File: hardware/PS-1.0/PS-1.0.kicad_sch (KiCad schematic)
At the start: 46 parts, among them J1 Conn_02x16_Odd_Even, J2 Conn_01x05, J3 Conn_01x05, J8 Conn_01x03, J9 Conn_01x03, K1 RAYEX-L90, K2 RAYEX-L90, Q1 IRFPE50, Q2 IRFPE50, Q3 IRFPE50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

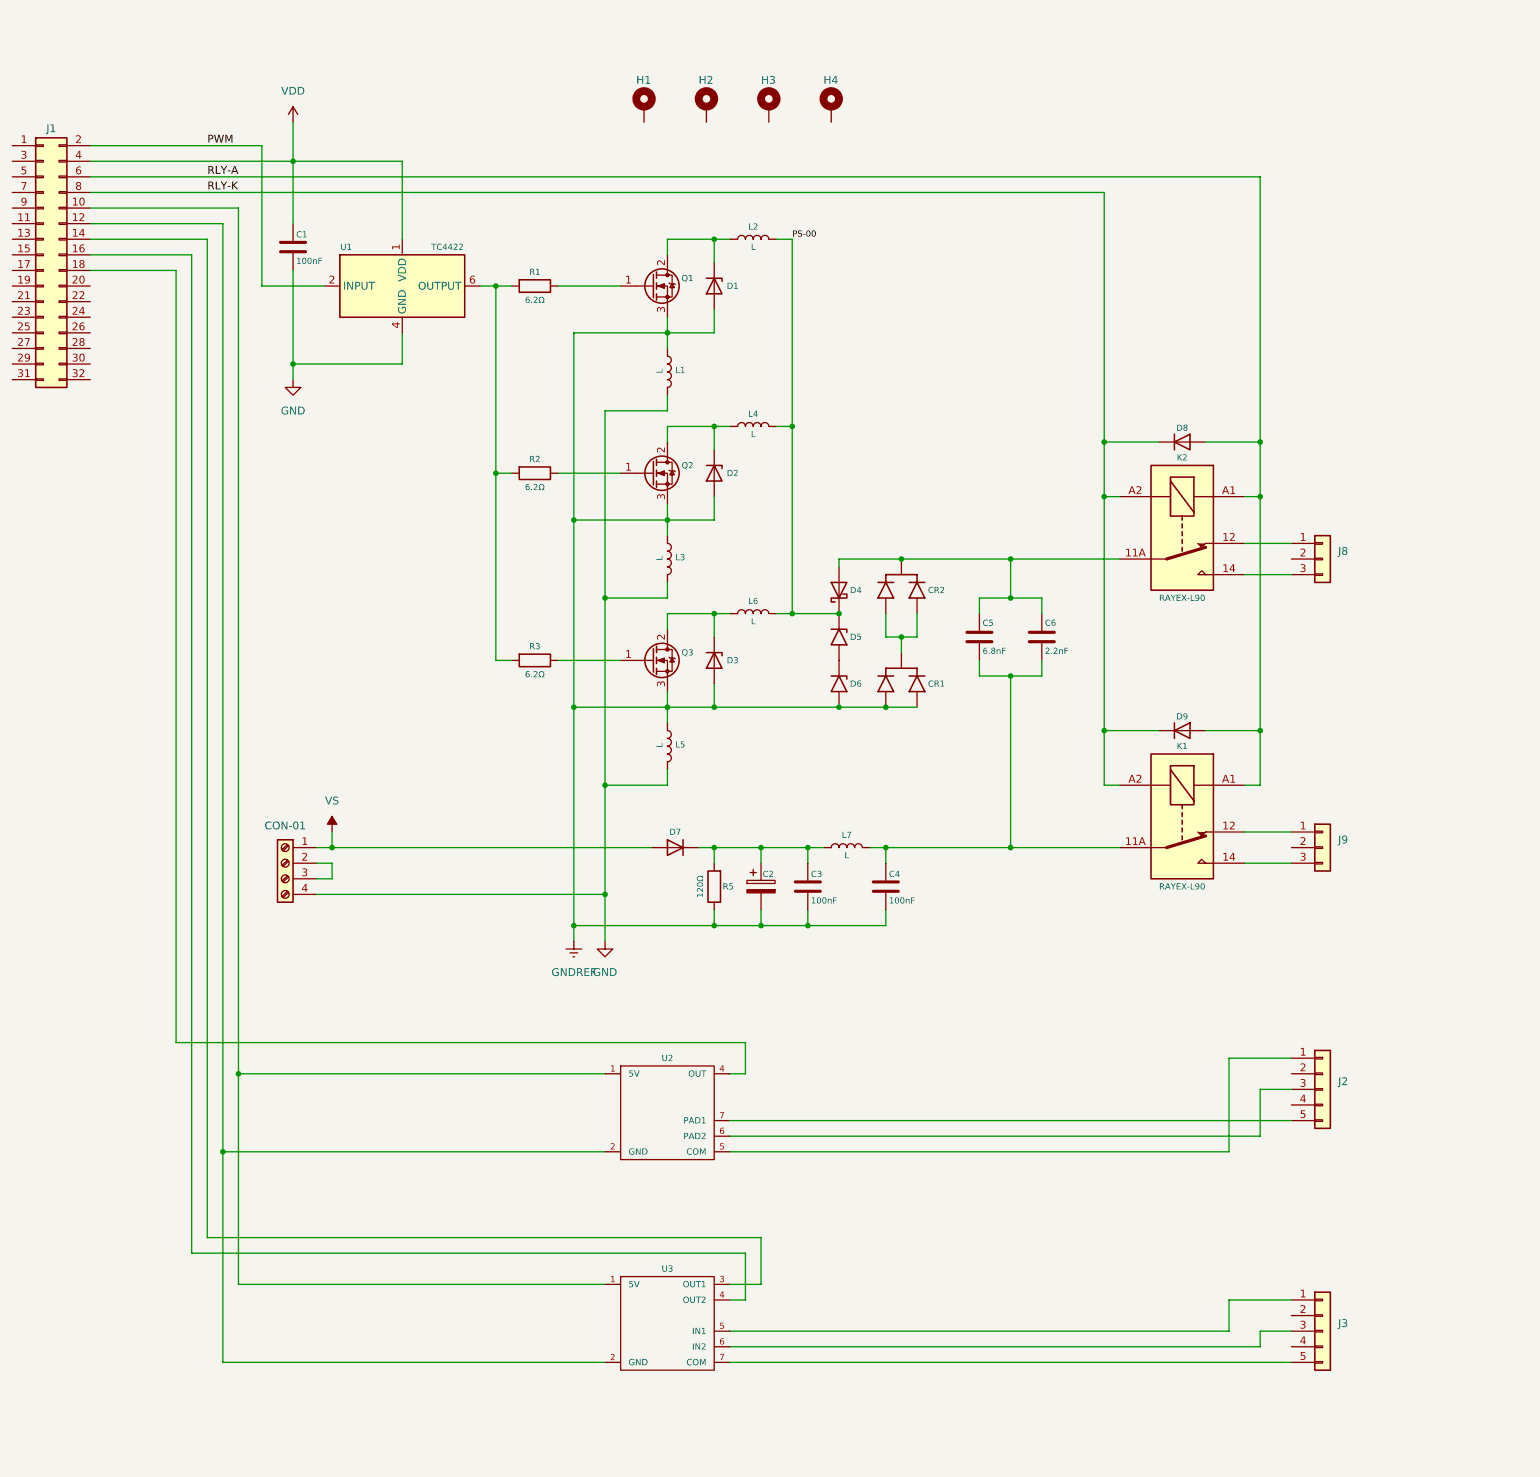
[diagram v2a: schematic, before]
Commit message: new file:   hardware/Gain/Gain-backups/Gain-2025-04-17_151501.zip 	deleted:    hardware/MSD-1.0/MSD-1.0-backups/MSD-1.0-2025-03-25_151318.zip 	deleted:    hardware/MSD-1.0/MSD-1.0-backups/MSD-1.0-2025-03-26_084506.zip 	deleted:    hardware/MSD-1.0/MSD-1.0-backups/MSD-1.0-2025-03-26_085636.zip 	deleted:    hardware/MSD-1.0/MSD-1.0-backups/MSD-1.0-2025-03-26_090649.zip 	new file:   hardware/MSD-1.0/MSD-1.0-backups/MSD-1.0-2025-04-17_090027.zip 	new file:   hardware/MSD-1.0/MSD-1.0-backups/MSD-1.0-2025-04-17_092653.zip 	new file:   hardware/MSD-1.0/MSD-1.0-backups/MSD-1.0-2025-04-17_105503.zip 	new file:   hardware/MSD-1.0/MSD-1.0-backups/MSD-1.0-2025-04-17_154051.zip 	modified:   hardware/MSD-1.0/MSD-1.0.kicad_pcb 	modified:   hardware/MSD-1.0/MSD-1.0.step 	deleted:    hardware/PS-1.0/PS-1.0-backups/PS-1.0-2025-03-19_103853.zip 	deleted:    hardware/PS-1.0/PS-1.0-backups/PS-1.0-2025-03-19_155128.zip 	deleted:    hardware/PS-1.0/PS-1.0-backups/PS-1.0-2025-03-24_095559.zip 	deleted:    hardware/PS-1.0/PS-1.0-backups/PS-1.0-2025-03-24_110339.zip 	deleted:    hardware/PS-1.0/PS-1.0-backups/PS-1.0-2025-03-24_111100.zip 	deleted:    hardware/PS-1.0/PS-1.0-backups/PS-1.0-2025-04-16_154157.zip 	deleted:    hardware/PS-1.0/PS-1.0-backups/PS-1.0-2025-04-16_154838.zip 	new file:   hardware/PS-1.0/PS-1.0-backups/PS-1.0-2025-04-16_163259.zip 	new file:   hardware/PS-1.0/PS-1.0-backups/PS-1.0-2025-04-17_105409.zip 	new file:   hardware/PS-1.0/PS-1.0-backups/PS-1.0-2025-04-17_110908.zip 	new file:   hardware/PS-1.0/PS-1.0-backups/PS-1.0-2025-04-17_114838.zip 	new file:   hardware/PS-1.0/PS-1.0-backups/PS-1.0-2025-04-17_155117.zip 	new file:   hardware/PS-1.0/PS-1.0-backups/PS-1.0-2025-04-17_155935.zip 	new file:   hardware/PS-1.0/PS-1.0-backups/PS-1.0-2025-04-17_160519.zip 	modified:   hardware/PS-1.0/PS-1.0.kicad_pcb 	modified:   hardware/PS-1.0/PS-1.0.kicad_prl 	modified:   hardware/PS-1.0/PS-1.0.kicad_pro 	modified:   hardware/PS-1.0/PS-1.0.kicad_sch 	modified:   hardware/PS-1.0/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
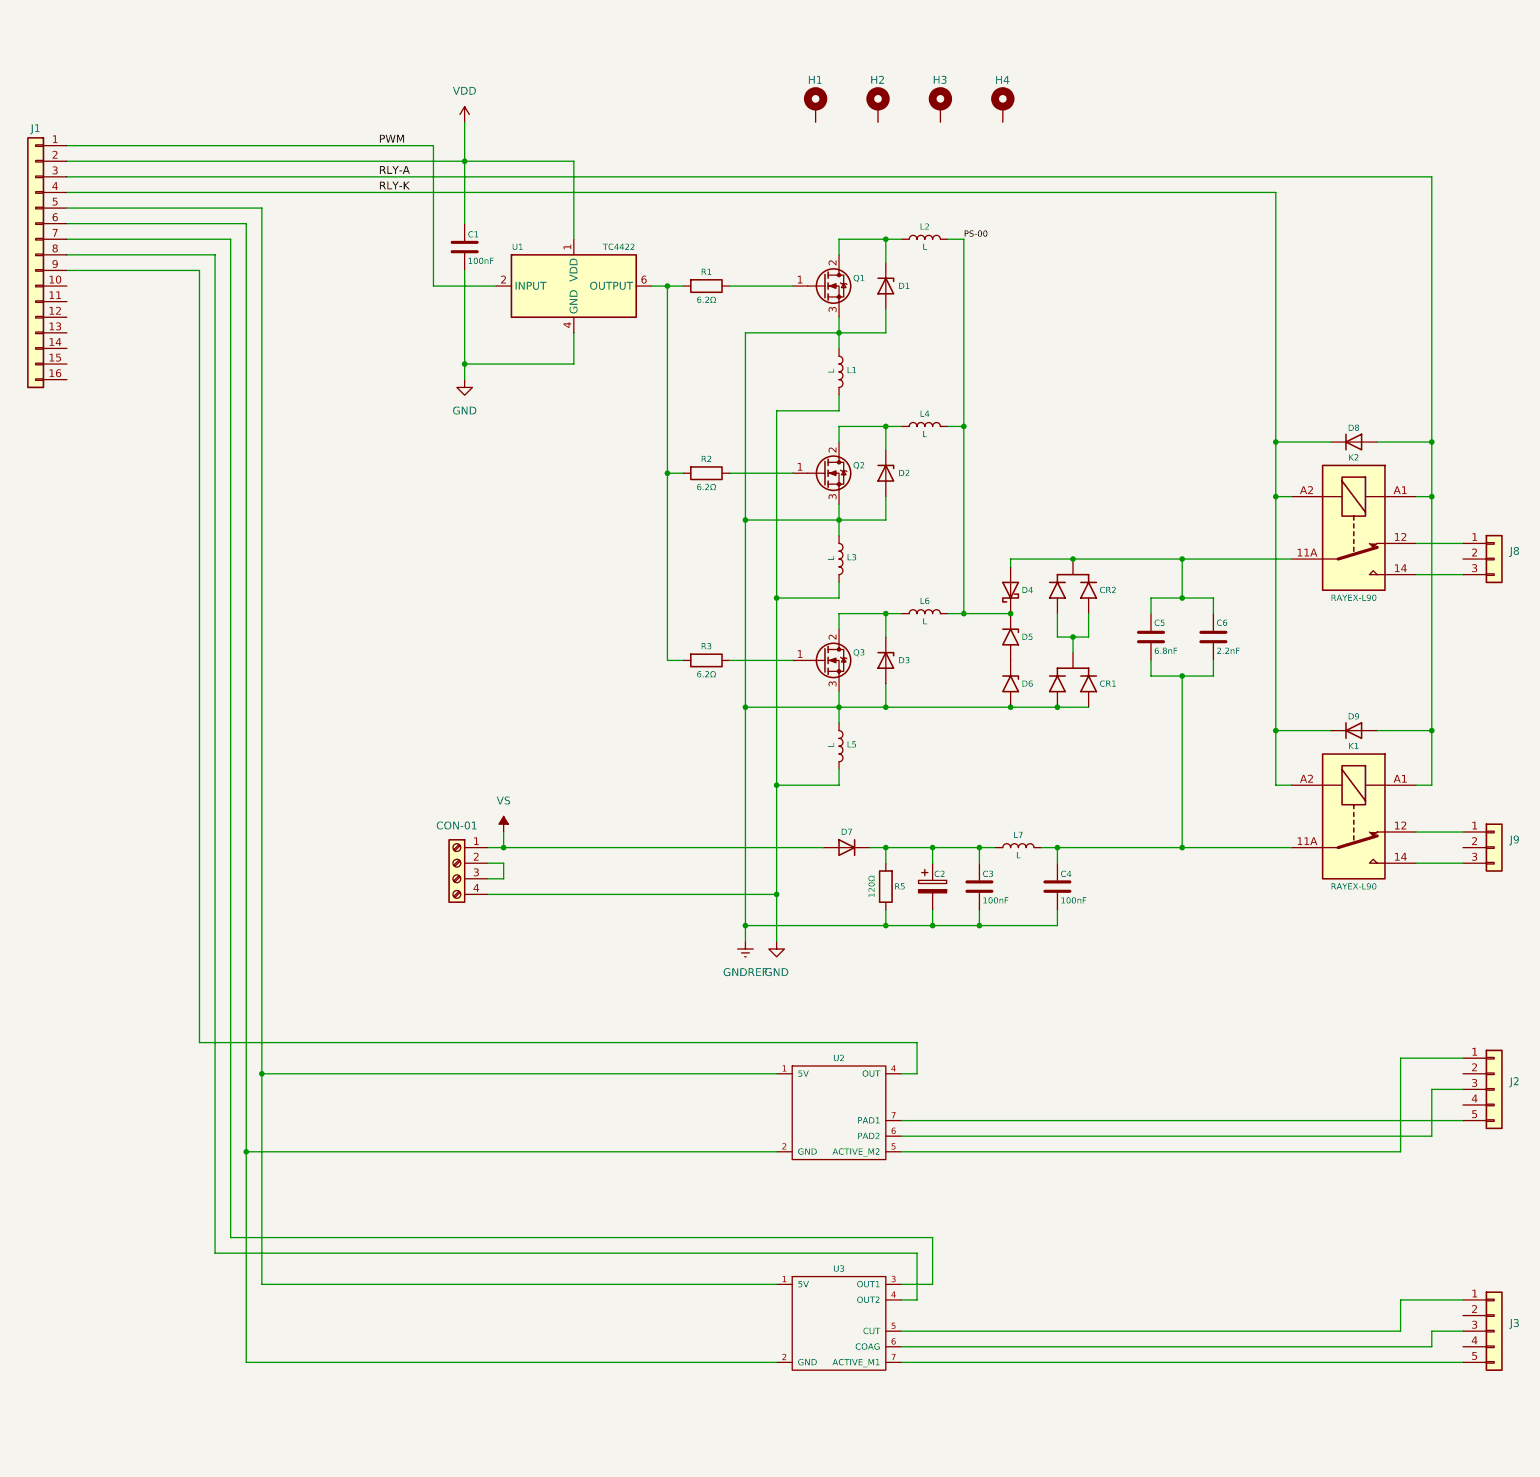
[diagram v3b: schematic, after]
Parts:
- removed J1: Conn_02x16_Odd_Even, Connector_PinSocket_2.54mm:PinSocket_2x16_P2.54mm_Vertical, symbol Connector_Generic:Conn_02x16_Odd_Even
- added J1: Conn_01x16, Connector_PinSocket_2.54mm:PinSocket_1x16_P2.54mm_Vertical_2, symbol Connector_Generic:Conn_01x16
- U2: footprint Custom:ESU-REM-3.0 -> Custom:ESU-REM-4.0; symbol Custom:ESU-REM-3.0 -> Custom:ESU-REM-4.0
- U3: footprint Custom:ESU-REM-3.0 -> Custom:ESU-MSD-1.0
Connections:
- net PWM: now also J1.1 (Pin_1)
- net RLY-A: now also J1.3 (Pin_3)
- net RLY-K: now also J1.4 (Pin_4)
- net VDD: now also J1.2 (Pin_2)
- net at U2.1 (5V), U3.1 (5V): now also J1.5 (Pin_5)
- net at U2.2 (GND), U3.2 (GND): now also J1.6 (Pin_6)
- net at U3.3 (OUT1): now also J1.7 (Pin_7)
- net at U3.4 (OUT2): now also J1.8 (Pin_8)
- net at U2.4 (OUT): now also J1.9 (Pin_9)
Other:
- moved on the sheet: C1, C2, C3, C4, C5, C6, CON-01, CR1, CR2, D1, D2, D3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

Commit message: new file:   .~BoM.xlsx 	new file:   BoM.xlsx 	new file:   hardware/BoM.xlsx 	deleted:    hardware/MSD-1.0/MSD-1.0-backups/MSD-1.0-2025-03-26_092035.zip 	deleted:    hardware/MSD-1.0/MSD-1.0-backups/MSD-1.0-2025-03-26_092834.zip 	deleted:    hardware/MSD-1.0/MSD-1.0-backups/MSD-1.0-2025-03-27_092014.zip 	new file:   hardware/MSD-1.0/MSD-1.0-backups/MSD-1.0-2025-04-28_130614.zip 	new file:   hardware/MSD-1.0/MSD-1.0-backups/MSD-1.0-2025-04-28_131128.zip 	new file:   hardware/MSD-1.0/MSD-1.0-backups/MSD-1.0-2025-04-28_132753.zip 	new file:   hardware/MSD-1.0/MSD-1.0.csv 	modified:   hardware/MSD-1.0/MSD-1.0.kicad_pcb 	modified:   hardware/MSD-1.0/MSD-1.0.kicad_sch 	deleted:    hardware/PS-1.0/PS-1.0-backups/PS-1.0-2025-03-24_111800.zip 	deleted:    hardware/PS-1.0/PS-1.0-backups/PS-1.0-2025-03-24_112738.zip 	deleted:    hardware/PS-1.0/PS-1.0-backups/PS-1.0-2025-03-25_152833.zip 	deleted:    hardware/PS-1.0/PS-1.0-backups/PS-1.0-2025-03-25_154601.zip 	deleted:    hardware/PS-1.0/PS-1.0-backups/PS-1.0-2025-03-25_155821.zip 	deleted:    hardware/PS-1.0/PS-1.0-backups/PS-1.0-2025-04-11_101418.zip 	deleted:    hardware/PS-1.0/PS-1.0-backups/PS-1.0-2025-04-11_110528.zip 	deleted:    hardware/PS-1.0/PS-1.0-backups/PS-1.0-2025-04-11_111527.zip 	deleted:    hardware/PS-1.0/PS-1.0-backups/PS-1.0-2025-04-11_114252.zip 	deleted:    hardware/PS-1.0/PS-1.0-backups/PS-1.0-2025-04-17_105409.zip 	new file:   hardware/PS-1.0/PS-1.0-backups/PS-1.0-2025-04-19_071925.zip 	new file:   hardware/PS-1.0/PS-1.0-backups/PS-1.0-2025-04-27_222808.zip 	new file:   hardware/PS-1.0/PS-1.0-backups/PS-1.0-2025-04-27_223939.zip 	new file:   hardware/PS-1.0/PS-1.0-backups/PS-1.0-2025-04-27_224445.zip 	new file:   hardware/PS-1.0/PS-1.0-backups/PS-1.0-2025-04-27_225206.zip 	new file:   hardware/PS-1.0/PS-1.0-backups/PS-1.0-2025-04-27_230217.zip 	new file:   hardware/PS-1.0/PS-1.0-backups/PS-1.0-2025-04-28_083014.zip 	new file:   hardware/PS-1.0/PS-1.0-backups/PS-1.0-2025-04-28_112951.zip 	new file:   har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
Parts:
- added R4: 100kΩ, Resistor_THT:R_Axial_DIN0204_L3.6mm_D1.6mm_P7.62mm_Horizontal, symbol Device:R
- added U4: PC817, Package_DIP:DIP-4_W7.62mm_Socket, symbol Isolator:PC817
- C2: value C_Polarized -> 1000µF 160V
- C3, C4: value 100nF -> 100nF 100V
- CON-01: value Screw_Terminal_01x04 -> KF7.62-4
- CR1, CR2: value ~ -> STTH1002CT
- D1, D2, D3: value 1N47xxA -> 1N4746A
- D4: value SB5H100 -> SB5H100/ SB5100
- D5, D6: value 1.5KExxA -> 1.5KE56A
- J1: value Conn_01x16 -> PinSocket_02x16_P2.54mm_Vertical
- R1, R2, R3: value 6.2Ω -> 6.2Ω 2W
- R5: value 120Ω -> 120Ω 2W
- U1: value TC4422 -> TC4422/ TC4420
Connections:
- net GND: now also J1.16 (Pin_16), U4.2, U4.3
- net at C2.1, C3.1, D7.1 (K)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: now also R4.2
- net at J1.10 (Pin_10): now also U4.4
- net at J1.15 (Pin_15): now also CON-01.2 (Pin_2), CON-01.3 (Pin_3)
- new net: R4.1, U4.1
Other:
- moved on the sheet: C2, C3, C4, CON-01, D7, J2, J3, L7, R5, U2, U3

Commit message: modified:   .DS_Store 	modified:   BoM.xlsx 	modified:   hardware/MSD-1.0/MSD-1.0-B_Cu.gbr 	modified:   hardware/MSD-1.0/MSD-1.0-B_Mask.gbr 	modified:   hardware/MSD-1.0/MSD-1.0-B_Paste.gbr 	modified:   hardware/MSD-1.0/MSD-1.0-B_Silkscreen.gbr 	modified:   hardware/MSD-1.0/MSD-1.0-Edge_Cuts.gbr 	modified:   hardware/MSD-1.0/MSD-1.0-F_Cu.gbr 	modified:   hardware/MSD-1.0/MSD-1.0-F_Mask.gbr 	modified:   hardware/MSD-1.0/MSD-1.0-F_Paste.gbr 	modified:   hardware/MSD-1.0/MSD-1.0-F_Silkscreen.gbr 	modified:   hardware/MSD-1.0/MSD-1.0-NPTH.drl 	modified:   hardware/MSD-1.0/MSD-1.0-PTH.drl 	deleted:    hardware/MSD-1.0/MSD-1.0-backups/MSD-1.0-2025-04-08_105747.zip 	new file:   hardware/MSD-1.0/MSD-1.0-backups/MSD-1.0-2025-04-29_135016.zip 	modified:   hardware/MSD-1.0/MSD-1.0-job.gbrjob 	modified:   hardware/MSD-1.0/MSD-1.zip 	new file:   hardware/PS-1.0/PS-1.0-B_Cu.gbr 	new file:   hardware/PS-1.0/PS-1.0-B_Mask.gbr 	new file:   hardware/PS-1.0/PS-1.0-B_Paste.gbr 	new file:   hardware/PS-1.0/PS-1.0-B_Silkscreen.gbr 	new file:   hardware/PS-1.0/PS-1.0-Edge_Cuts.gbr 	new file:   hardware/PS-1.0/PS-1.0-F_Cu.gbr 	new file:   hardware/PS-1.0/PS-1.0-F_Mask.gbr 	new file:   hardware/PS-1.0/PS-1.0-F_Paste.gbr 	new file:   hardware/PS-1.0/PS-1.0-F_Silkscreen.gbr 	new file:   hardware/PS-1.0/PS-1.0-NPTH.drl 	new file:   hardware/PS-1.0/PS-1.0-PTH.drl 	deleted:    hardware/PS-1.0/PS-1.0-backups/PS-1.0-2025-04-11_131644.zip 	deleted:    hardware/PS-1.0/PS-1.0-backups/PS-1.0-2025-04-14_085622.zip 	deleted:    hardware/PS-1.0/PS-1.0-backups/PS-1.0-2025-04-14_104133.zip 	deleted:    hardware/PS-1.0/PS-1.0-backups/PS-1.0-2025-04-14_105043.zip 	deleted:    hardware/PS-1.0/PS-1.0-backups/PS-1.0-2025-04-14_110044.zip 	deleted:    hardware/PS-1.0/PS-1.0-backups/PS-1.0-2025-04-16_155906.zip 	deleted:    hardware/PS-1.0/PS-1.0-backups/PS-1.0-2025-04-16_160456.zip 	new file:   hardware/PS-1.0/PS-1.0-backups/PS-1.0-2025-04-29_112020.zip 	new file:   hardware/PS-1.0/PS-1.0-backups/PS-1.0-2025-04-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
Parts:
- added HS1, HS2: Heatsink, Heatsink:Heatsink_Stonecold_HS-132_32x14mm_2xFixation1.5mm_NoPad, symbol Mechanical:Heatsink
- added HS3: Heatsink, Heatsink:Heatsink_Custom_10x18x50, symbol Mechanical:Heatsink
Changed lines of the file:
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@@
+	)
+	(symbol
+		(lib_id "Mechanical:Heatsink")
+		(at 124.46 43.18 0)
+		(unit 1)
+		(exclude_from_sim yes)
+		(in_bom yes)
+		(on_board yes)
+		(dnp no)
+		(property "Reference" "HS1"
+			(at 124.46 38.1 0)
+			(effects
+				(font
+					(size 1.27 1.27)
+				)
+			)
+		)
+		(property "Value" "Heatsink"
+			(at 128.27 42.5449 0)
+			(effects
+				(font
+					(size 1.27 1.27)
+				)
+				(justify left)
+				(hide yes)
+			)
+		)
+		(property "Footprint" "Heatsink:Heatsink_Stonecold_HS-132_32x14mm_2xFixation1.5mm_NoPad"
+			(at 124.7648 43.18 0)
+			(effects
+				(font
+					(size 1.27 1.27)
+				)
+				(hide yes)
+			)
+		)
+		(property "Datasheet" "~"
+			(at 124.7648 43.18 0)
+			(effects
+				(font
+					(size 1.27 1.27)
+				)
+				(hide yes)
+			)
+		)
+		(property "Description" "Heatsink"
+			(at 124.46 43.18 0)
+			(effects
+				(font
+					(size 1.27 1.27)
+				)
+				(hide yes)
+			)
+		)
+		(instances
+			(project ""
+				(path "/3a4da535-700d-4512-9d93-355e5c375ab5"
+					(reference "HS1")
+					(unit 1)
+				)
+			)
+		)
 	)
 	(symbol
@@
 	)
 	(symbol
+		(lib_id "Mechanical:Heatsink")
+		(at 139.7 43.18 0)
+		(unit 1)
+		(exclude_from_sim yes)
+		(in_bom yes)
+		(on_board yes)
+		(dnp no)
+		(property "Reference" "HS3"
+			(at 139.7 38.1 0)
+			(effects
+				(font
+					(size 1.27 1.27)
+				)
+			)
+		)
+		(property "Value" "Heatsink"
+			(at 143.51 42.5449 0)
+			(effects
+				(font
+					(size 1.27 1.27)
+				)
+				(justify left)
+				(hide yes)
+			)
+		)
+		(property "Footprint" "Heatsink:Heatsink_Custom_10x18x50"
+			(at 140.0048 43.18 0)
+			(effects
+				(font
+					(size 1.27 1.27)
+				)
+				(hide yes)
+			)
+		)
+		(property "Datasheet" "~"
+			(at 140.0048 43.18 0)
+			(effects
+				(font
+					(size 1.27 1.27)
+				)
+				(hide yes)
+			)
+		)
+		(property "Description" "Heatsink"
+			(at 139.7 43.18 0)
+			(effects
+				(font
+					(size 1.27 1.27)
+				)
+				(hide yes)
+			)
+		)
+		(instances
+			(project "PS-1.0"
+				(path "/3a4da535-700d-4512-9d93-355e5c375ab5"
+					(reference "HS3")
+					(unit 1)
+				)
+			)
+		)
+	)
+	(symbol
 		(lib_id "Device:L")
 		(at 160.02 115.57 0)
@@
 					(unit 1)
 				)
+			)
+		)
+	)
+	(symbol
+		(lib_id "Mechanical:Heatsink")
+		(at 132.08 43.18 0)
+		(unit 1)
+		(exclude_from_sim yes)
+		(in_bom yes)
+		(on_board yes)
+		(dnp no)
+		(property "Reference" "HS2"
+			(at 132.08 38.1 0)
+			(effects
+				(font
+					(size 1.27 1.27)
+				)
+			)
+		)
+		(property "Value" "Heatsink"
+			(at 135.89 42.5449 0)
+			(effects
+				(font
+					(size 1.27 1.27)
+				)
+				(justify left)
+				(hide yes)
+			)
+		)
+		(property "Footprint" "Heatsink:Heatsink_Stonecold_HS-132_32x14mm_2xFixation1.5mm_NoPad"
+			(at 132.3848 43.18 0)
+			(effects
+				(font
+					(size 1.27 1.27)
+				)
+				(hide yes)
+			)
+		)
+		(property "Datasheet" "~"
+			(at 132.3848 43.18 0)
+			(effects
+				(font
+					(size 1.27 1.27)
+				)
+				(hide yes)
+			)
+		)
+		(property "Description" "Heatsink"
+			(at 132.08 43.18 0)
+			(effects
+				(font
+					(size 1.27 1.27)
+				)
+				(hide yes)
+			)
+		)
+		(instances
+			(project "PS-1.0"
+				(path "/3a4da535-700d-4512-9d93-355e5c375ab5"
+					(reference "HS2")
+					(unit 1)
+				)
